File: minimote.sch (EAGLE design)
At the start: 46 parts, among them IC1 ATTINY841, J1 AVR_SPI_PROG_3X2PTH, J2 EDGEUSB, Q1 SS8050, Q2 SI2301, U1 M24Cxx

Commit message: pause commit
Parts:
- added PAD1: (no value), wirepad:2,15/1,0
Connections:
- net PA1: now also PAD1.P
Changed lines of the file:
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@@
 <?xml version="1.0" encoding="utf-8"?>
 <!DOCTYPE eagle SYSTEM "eagle.dtd">
-<eagle version="8.6.3">
+<eagle version="8.7.1">
 <drawing>
 <settings>
@@
 <part name="GND10" library="supply1" library_urn="urn:adsk.eagle:library:371" deviceset="GND" device=""/>
 <part name="GND11" library="supply1" library_urn="urn:adsk.eagle:library:371" deviceset="GND" device=""/>
+<part name="PAD1" library="wirepad" library_urn="urn:adsk.eagle:library:412" deviceset="2,15/1,0" device="" package3d_urn="urn:adsk.eagle:package:30831/1"/>
 </parts>
 <sheets>
@@
 <instance part="GND10" gate="1" x="127" y="50.8"/>
 <instance part="GND11" gate="1" x="210.82" y="81.28"/>
+<instance part="PAD1" gate="1" x="109.22" y="20.32" rot="R180"/>
 </instances>
 <busses>
@@
 <segment>
 <pinref part="IC1" gate="IC1" pin="(PCINT1/ADC1/AIN00/TOCC0/TXD0/MOSI)PA1"/>
-<wire x1="78.74" y1="27.94" x2="99.06" y2="27.94" width="0.1524" layer="91"/>
+<wire x1="78.74" y1="27.94" x2="104.14" y2="27.94" width="0.1524" layer="91"/>
 <label x="83.82" y="27.94" size="1.778" layer="95"/>
-</segment>
-</net>
+<wire x1="104.14" y1="27.94" x2="104.14" y2="20.32" width="0.1524" layer="91"/>
+<pinref part="PAD1" gate="1" pin="P"/>
+<wire x1="104.14" y1="20.32" x2="106.68" y2="20.32" width="0.1524" layer="91"/>
+</segment>
+</net>

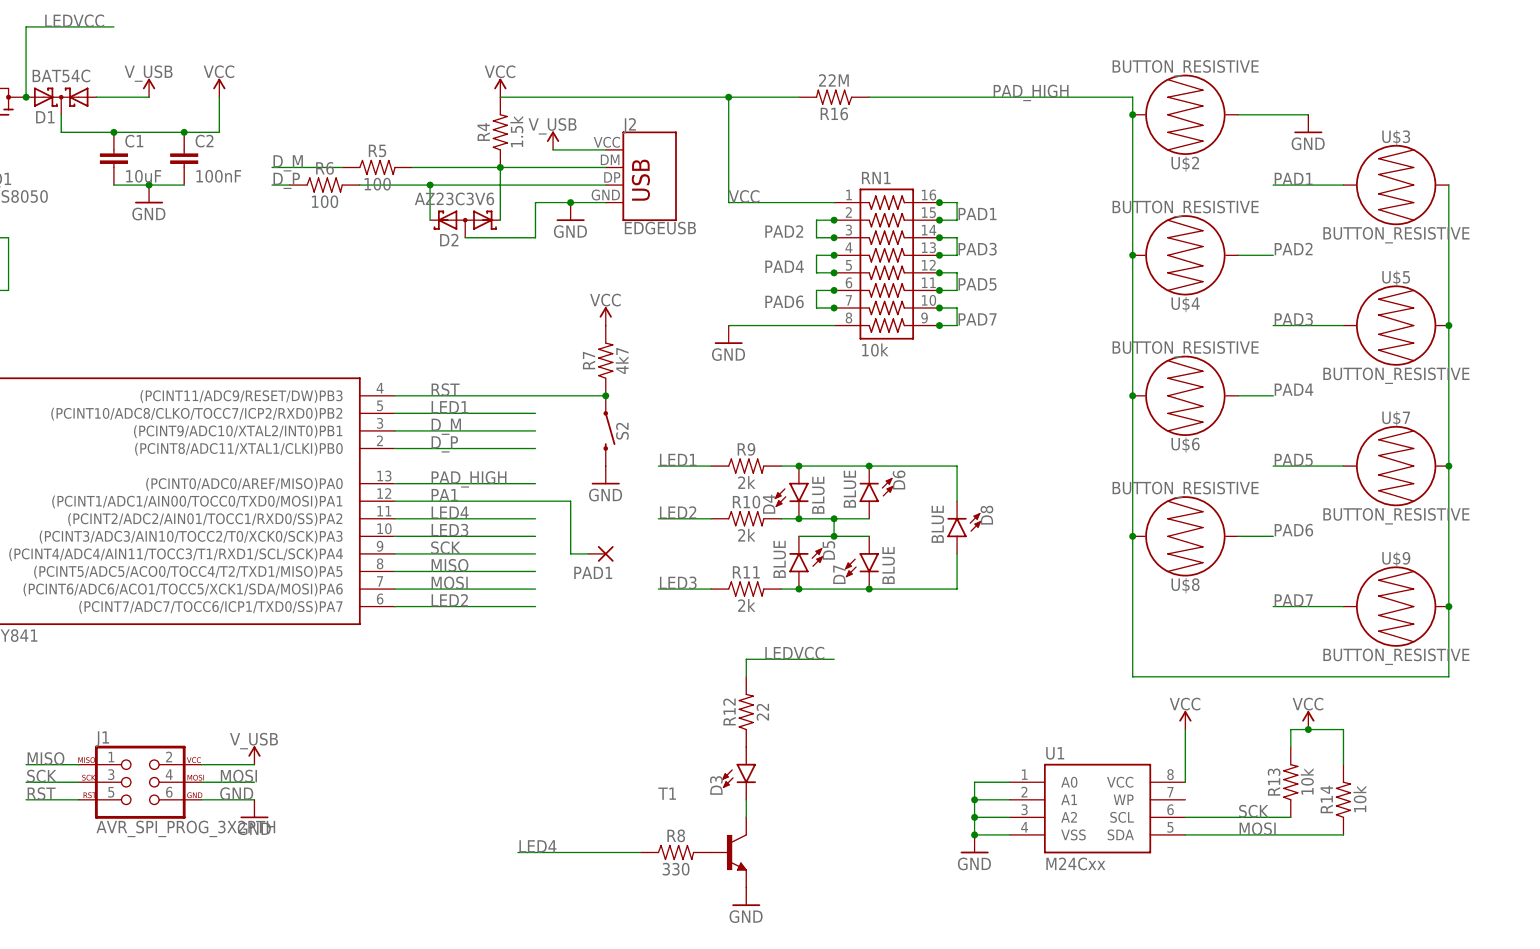
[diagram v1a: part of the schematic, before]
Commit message: routed new board
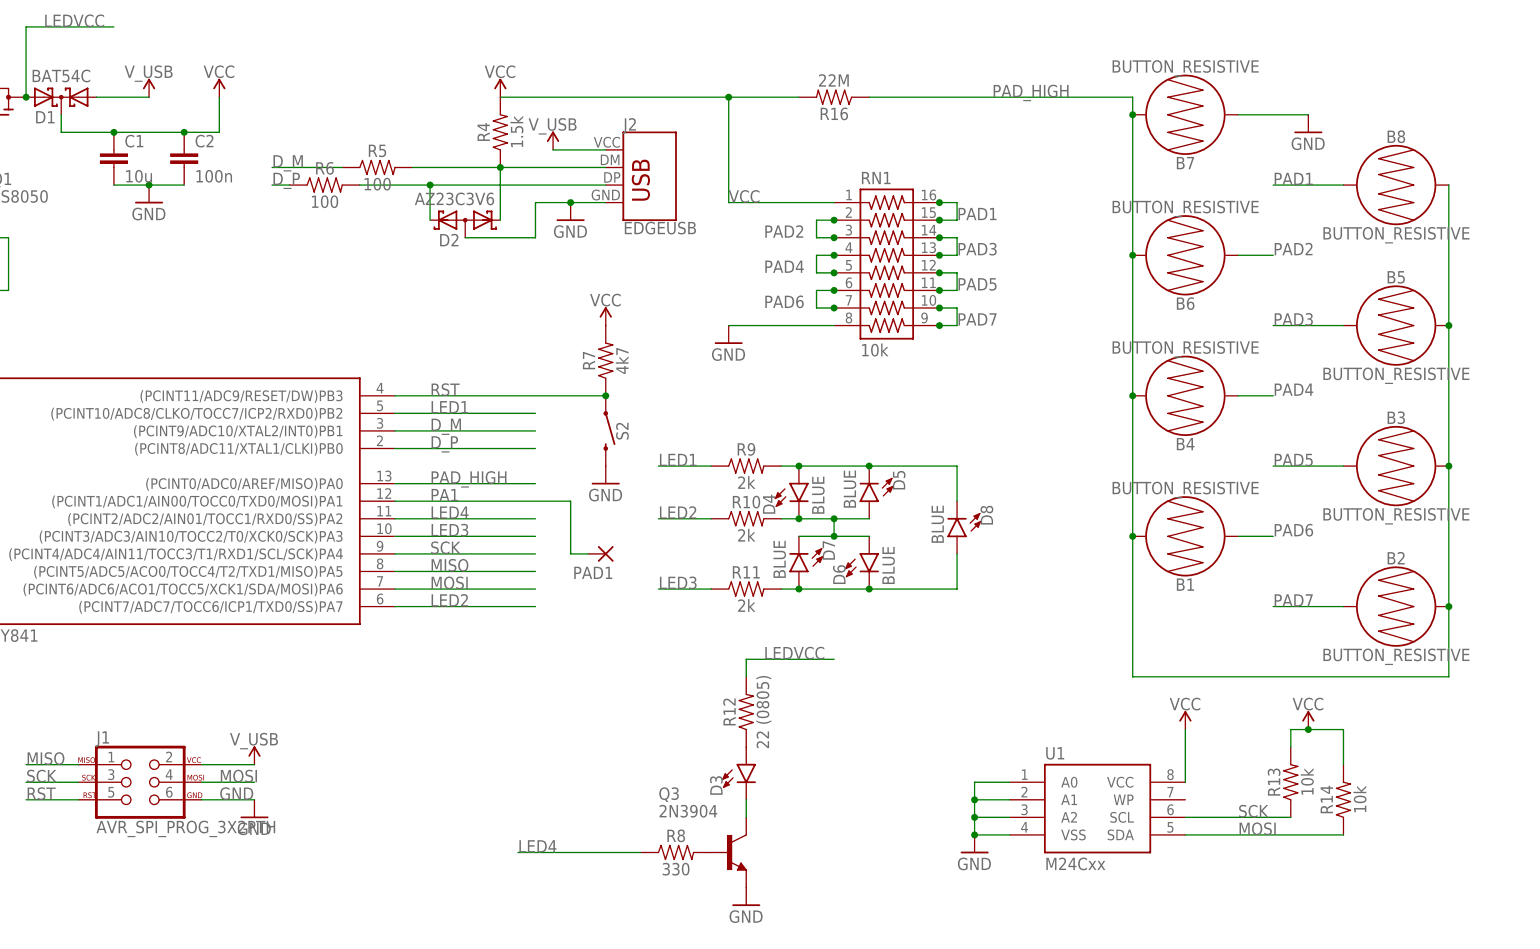
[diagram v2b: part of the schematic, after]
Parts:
- C1: value 10uF -> 10u
- C2: value 100nF -> 100n
- Q3: value (none) -> 2N3904
- R12: value 22 -> 22 (0805)
- renumbered T1 to Q3, U$2 to B7, U$3 to B8, U$4 to B6, U$5 to B5, U$6 to B4, U$7 to B3, U$8 to B1, U$9 to B2
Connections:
- net N$123: now also D6.C, D7.A; no longer D5.A, D7.C
- net N$124: now also D5.A, D7.C; no longer D5.C, D7.A
- net N$125: now also D5.C; no longer D6.C
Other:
- moved on the sheet: D5, D6, D7

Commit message: Rev 2 board sent to OSHPark
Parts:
- removed FRAME1: FRAME-LEDGER, SparkFun-Aesthetics:FRAME-LEDGER
- removed PAD1: (no value), wirepad:2,15/1,0
- added U$2: TSOP1837, tsop:TSOP1837
- J1: device SparkFun-Connectors:AVR_SPI_PROG_3X2PTH -> minimote:AVR_SPI_PROG_3X2PTH
- renumbered S2 to RST
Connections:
- removed net PA1: IC1.(PCINT1/ADC1/AIN00/TOCC0/TXD0/MOSI)PA1, PAD1.P
- new net RECV: IC1.(PCINT1/ADC1/AIN00/TOCC0/TXD0/MOSI)PA1, U$2.OUT
- net GND: now also U$2.GND
- net LEDVCC: now also U$2.V+
- net RST: now also J2.SENSE
